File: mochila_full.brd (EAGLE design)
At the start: 100 x 80 mm, 13 parts, among them IC1 AD620R

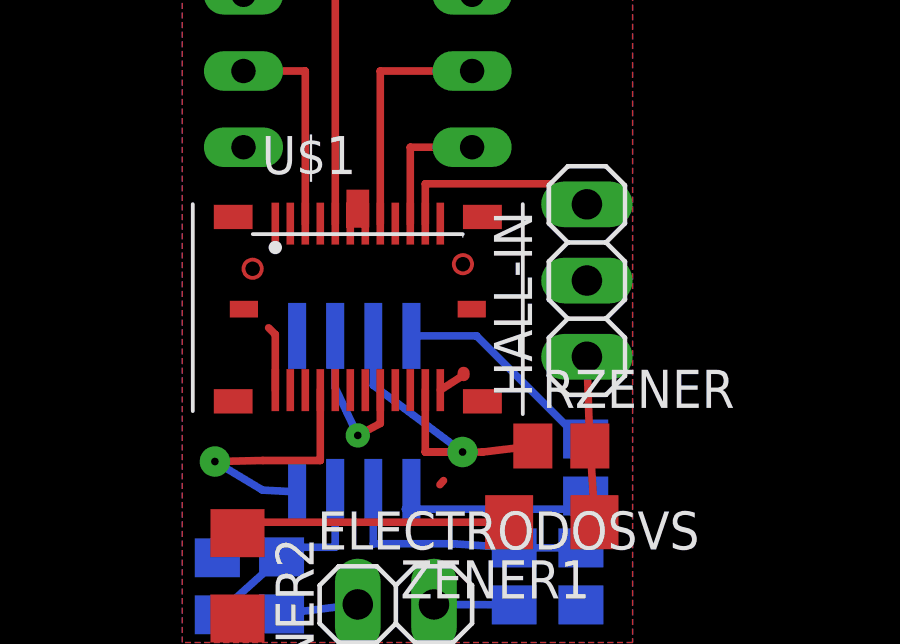
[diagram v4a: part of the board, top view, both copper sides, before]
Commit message: Usamos nueva libreria USBC
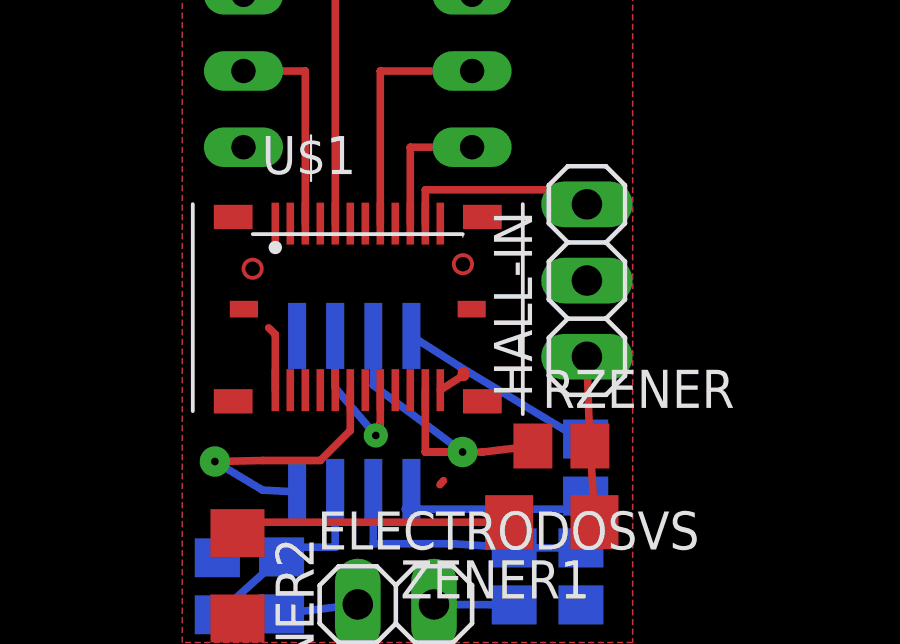
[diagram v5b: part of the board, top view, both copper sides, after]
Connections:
- removed net N$24: U$1.NC6
- net -12V: now also U$1.-12V; no longer U$1.-12VA, U$1.-12VB
- net EXTRA1: now also U$1.EXTRA1; no longer U$1.E1
- net EXTRA2: now also U$1.EXTRA2; no longer U$1.E2
- net N$12: now also U$1.ANULADA1; no longer U$1.CHECK1
- net N$13: now also U$1.ANULADA2; no longer U$1.CHECK2
- net N$25: now also U$1.EXTRA4; no longer U$1.NC5
- net NC2: now also U$1.EXTRA3C; no longer U$1.NC2
- net NC3: now also U$1.EXTRA3D; no longer U$1.NC4
- net OUTT: now also U$1.OUTT; no longer U$1.T
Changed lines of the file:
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@@
 <?xml version="1.0" encoding="utf-8"?>
 <!DOCTYPE eagle SYSTEM "eagle.dtd">
-<eagle version="9.2.2">
+<eagle version="7.7.0">
 <drawing>
 <settings>
 <setting alwaysvectorfont="no"/>
-<setting keepoldvectorfont="yes"/>
 <setting verticaltext="up"/>
 </settings>
@@
 <param name="dpMaxLengthDifference" value="10mm"/>
 <param name="dpGapFactor" value="2.5"/>
+<param name="checkGrid" value="0"/>
 <param name="checkAngle" value="0"/>
 <param name="checkFont" value="1"/>
 <param name="checkRestrict" value="1"/>
-<param name="checkStop" value="0"/>
-<param name="checkValues" value="0"/>
-<param name="checkNames" value="1"/>
-<param name="checkWireStubs" value="1"/>
-<param name="checkPolygonWidth" value="0"/>
 <param name="useDiameter" value="13"/>
 <param name="maxErrors" value="50"/>
@@
 <wire x1="37.5" y1="25.5" x2="36.7225" y2="30.4725" width="0" layer="19" extent="1-1"/>
 <wire x1="31.2225" y1="30.4725" x2="31" y2="27" width="0" layer="19" extent="1-1"/>
-<wire x1="41.41" y1="17.765" x2="36.83" y2="21.9075" width="0" layer="19" extent="1-16"/>
 </signal>
 <signal name="N$5">
@@
 <contactref element="IC1" pad="8"/>
 <wire x1="41.57" y1="23.2925" x2="41.37" y2="23.2925" width="0.254" layer="16"/>
-<wire x1="41.37" y1="23.2925" x2="37.9325" y2="26.73" width="0.254" layer="16"/>
-<wire x1="35.76" y1="26.73" x2="37.9325" y2="26.73" width="0.254" layer="16"/>
+<wire x1="41.37" y1="23.2925" x2="37.3325" y2="25.73" width="0.254" layer="16"/>
+<wire x1="35.76" y1="26.73" x2="37.3325" y2="25.73" width="0.254" layer="16"/>
 </signal>
 <signal name="+12V">
@@
 <signal name="-12V">
 <contactref element="IC1" pad="4"/>
-<contactref element="U$1" pad="-12VA"/>
-<contactref element="U$1" pad="-12VB"/>
 <wire x1="29.21" y1="22.5425" x2="30.81" y2="22.5775" width="0.254" layer="1"/>
 <wire x1="30.7975" y1="21.59" x2="29.21" y2="22.5425" width="0.254" layer="16"/>
 <wire x1="30.7975" y1="21.59" x2="31.95" y2="21.53" width="0.254" layer="16"/>
 <via x="29.21" y="22.5425" extent="1-16" drill="0.254" diameter="1.016" shape="square"/>
-<wire x1="32.7225" y1="24.9225" x2="32.7225" y2="22.5775" width="0.254" layer="1"/>
 <wire x1="32.7225" y1="22.5775" x2="30.81" y2="22.5775" width="0.254" layer="1"/>
-<wire x1="32.7225" y1="24.9225" x2="32.7225" y2="30.4725" width="0" layer="19" extent="1-1"/>
+<contactref element="U$1" pad="-12V"/>
+<wire x1="33.7225" y1="24.9225" x2="33.7225" y2="23.5775" width="0.254" layer="1"/>
+<wire x1="33.7225" y1="23.5775" x2="32.7225" y2="22.5775" width="0.254" layer="1"/>
 </signal>
 <signal name="OUTT">
 <contactref element="IC1" pad="6"/>
-<wire x1="33.22" y1="25" x2="33.9725" y2="23.4125" width="0.254" layer="16"/>
+<wire x1="33.22" y1="25" x2="34.5725" y2="23.4125" width="0.254" layer="16"/>
 <wire x1="33.22" y1="26.73" x2="33.22" y2="25" width="0.254" layer="16"/>
-<via x="33.9725" y="23.4125" extent="1-16" drill="0.254" diameter="0.8128" shape="square"/>
-<wire x1="33.9725" y1="23.4125" x2="34.7225" y2="23.8125" width="0.254" layer="1"/>
-<contactref element="U$1" pad="T"/>
+<via x="34.5725" y="23.4125" extent="1-16" drill="0.254" diameter="0.8128" shape="square"/>
+<wire x1="34.5725" y1="23.4125" x2="34.7225" y2="23.8125" width="0.254" layer="1"/>
+<contactref element="U$1" pad="OUTT"/>
 <wire x1="34.7225" y1="24.9225" x2="34.7225" y2="23.8125" width="0.254" layer="1"/>
 </signal>
@@
 </signal>
 <signal name="N$12">
-<contactref element="U$1" pad="CHECK1"/>
+<contactref element="U$1" pad="ANULADA1"/>
 </signal>
 <signal name="N$13">
-<contactref element="U$1" pad="CHECK2"/>
+<contactref element="U$1" pad="ANULADA2"/>
 </signal>
 <signal name="-I">
@@
 <contactref element="HALL-IN" pad="3"/>
 <contactref element="U$1" pad="HALL"/>
-<wire x1="36.2225" y1="30.4725" x2="36.2225" y2="31.8" width="0.254" layer="1"/>
-<wire x1="36.2225" y1="31.8" x2="40.4" y2="31.8" width="0.254" layer="1"/>
-<wire x1="40.4" y1="31.8" x2="40.4" y2="31.115" width="0.254" layer="1"/>
+<wire x1="36.2225" y1="30.4725" x2="36.2225" y2="31.6" width="0.254" layer="1"/>
+<wire x1="36.2225" y1="31.6" x2="40.4" y2="31.6" width="0.254" layer="1"/>
+<wire x1="40.4" y1="31.6" x2="40.4" y2="31.115" width="0.254" layer="1"/>
 <wire x1="40.4" y1="31.115" x2="41.61" y2="31.115" width="0.254" layer="1"/>
 </signal>
@@
 <contactref element="U$1" pad="NC7"/>
 </signal>
-<signal name="N$24">
-<contactref element="U$1" pad="NC6"/>
-</signal>
 <signal name="N$25">
-<contactref element="U$1" pad="NC5"/>
+<contactref element="U$1" pad="EXTRA4"/>
 </signal>
 <signal name="NC3">
-<contactref element="U$1" pad="NC4"/>
+<contactref element="U$1" pad="EXTRA3D"/>
 </signal>
 <signal name="+5V">
@@
 </signal>
 <signal name="EXTRA2">
-<contactref element="U$1" pad="E2"/>
+<contactref element="U$1" pad="EXTRA2"/>
 </signal>
 <signal name="NC2">
-<contactref element="U$1" pad="NC2"/>
+<contactref element="U$1" pad="EXTRA3C"/>
 </signal>
 <signal name="NC6">
@@
 </signal>
 <signal name="EXTRA1">
-<contactref element="U$1" pad="E1"/>
+<contactref element="U$1" pad="EXTRA1"/>
 </signal>
 </signals>
-<mfgpreviewcolors>
-<mfgpreviewcolor name="soldermaskcolor" color="0xC8008000"/>
-<mfgpreviewcolor name="silkscreencolor" color="0xFFFEFEFE"/>
-<mfgpreviewcolor name="backgroundcolor" color="0xFF282828"/>
-<mfgpreviewcolor name="coppercolor" color="0xFFFFBF00"/>
-<mfgpreviewcolor name="substratecolor" color="0xFF786E46"/>
-</mfgpreviewcolors>
 </board>
 </drawing>

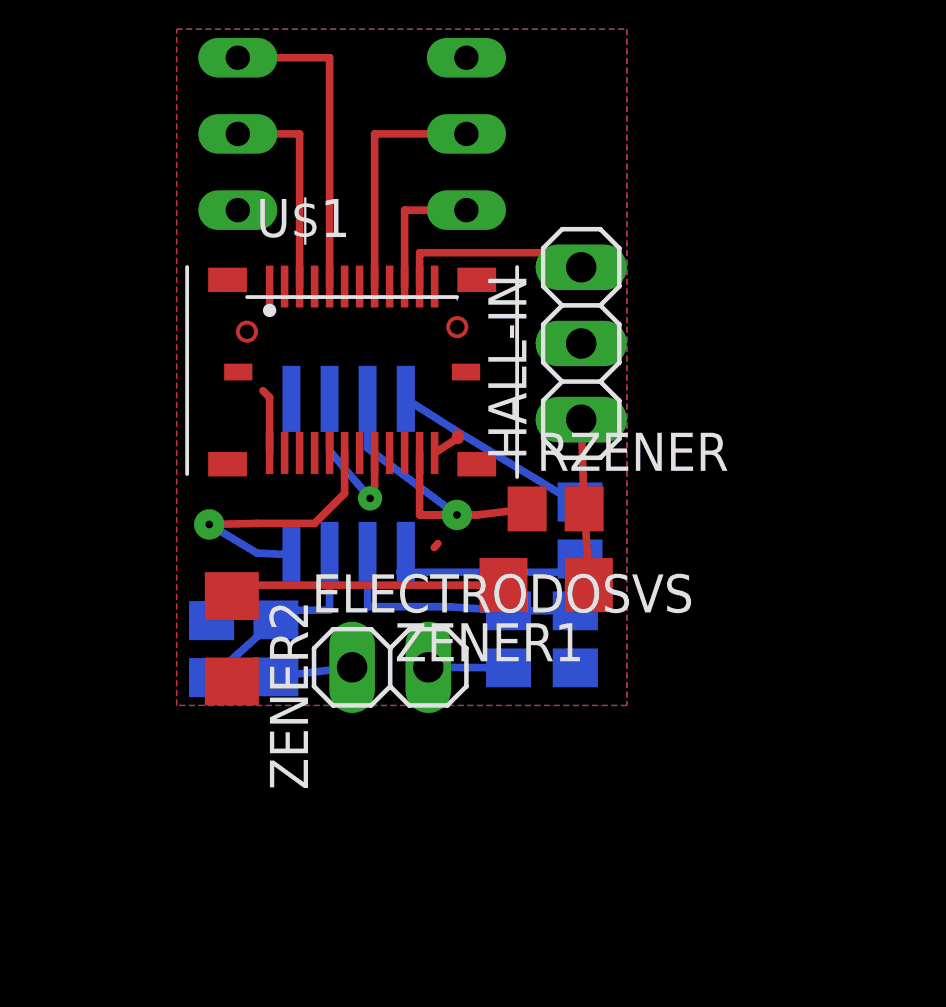
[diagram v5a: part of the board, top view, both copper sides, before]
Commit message: Version p/imprimir en masa
Reemplazo los zener por regulador 78L05

Agrego nombres y valores al layout
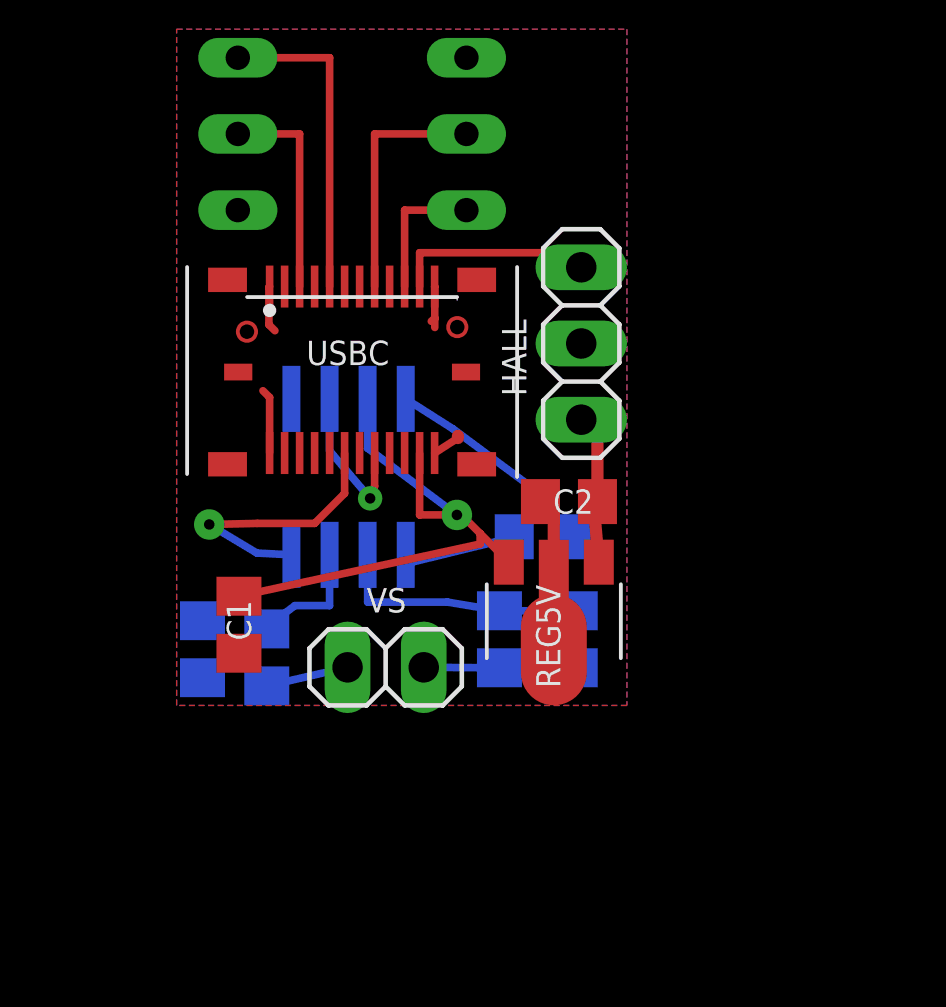
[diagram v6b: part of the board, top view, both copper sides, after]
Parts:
- removed CF1, CF2: (no value), eagle-ltspice:C0805
- removed ELECTRODOSVS: (no value), pinhead:1X02
- removed RF2, RZENER: (no value), eagle-ltspice:R0805
- removed ZENER1, ZENER2: (no value), eagle-ltspice:R1206
- added C1: 0.33u, rcl:C0805
- added C2: 0.1u, rcl:C0805
- added C3, C4: 10n, eagle-ltspice:C0805
- added R2: 100k, eagle-ltspice:R0805
- added REG5V: 78L05F, linear:SOT89
- added VS: (no value), pinhead:1X02
- R1: value (none) -> 100k
- RG: value (none) -> 220
- moved RG 1.26 mm to (40.3, 22.1), turned to 0 degrees
- renumbered FUJIKURASOCKET to FUJI, HALL-IN to HALL, RF1 to R1, U$1 to USBC
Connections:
- removed net N$8: ZENER1.2, ZENER2.1
- net +12V: now also C1.1, REG5V.3; no longer RZENER.1
- net +5V: now also C2.1, REG5V.1; no longer RZENER.2, ZENER1.1
- net GND: now also C1.2, C2.2, R2.1, REG5V.2; no longer RF2.1, ZENER2.2
- net N$1: now also C3.1, VS.1; no longer CF2.1, ELECTRODOSVS.1
- net N$2: now also C3.2, R2.2; no longer CF2.2, RF2.2
- net N$3: now also C4.1, VS.2; no longer CF1.1, ELECTRODOSVS.2
- net N$4: now also C4.2; no longer CF1.2
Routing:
- net N$8: track 9.67 -> 0.00 mm
- net +12V: track 12.3 -> 19.6 mm
- net GND: track 3.35 -> 8.76 mm
- net N$5: track 7.06 -> 3.91 mm

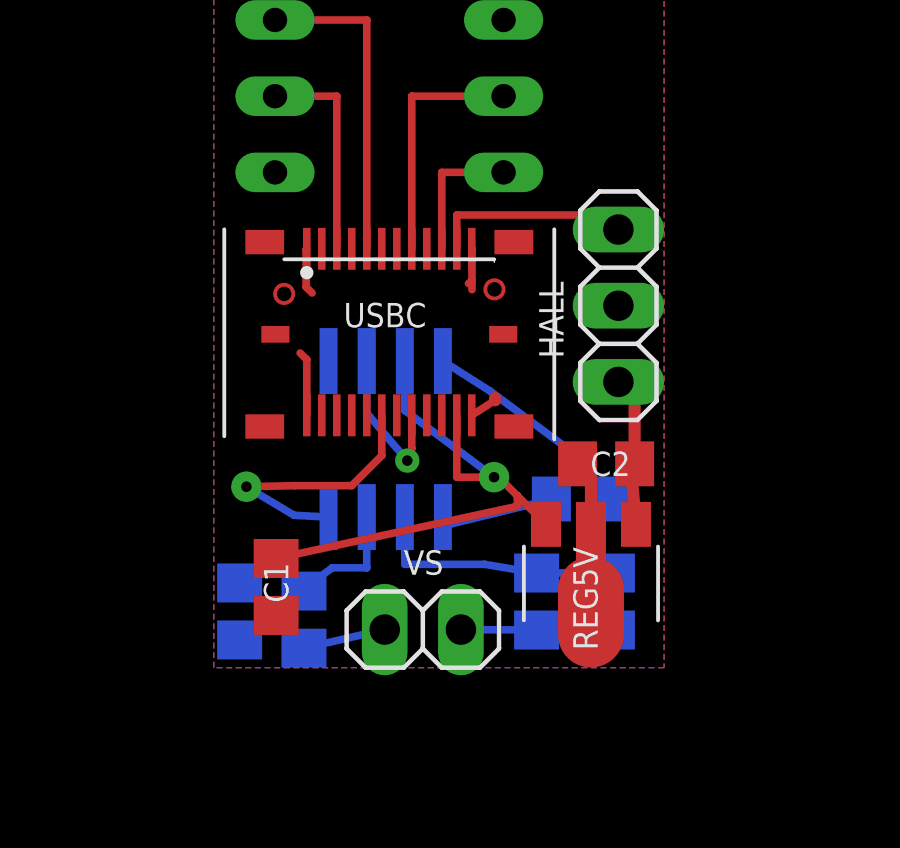
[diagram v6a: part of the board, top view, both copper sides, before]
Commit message: Version para imprimir de la mochila, con gerbers generados en .zip
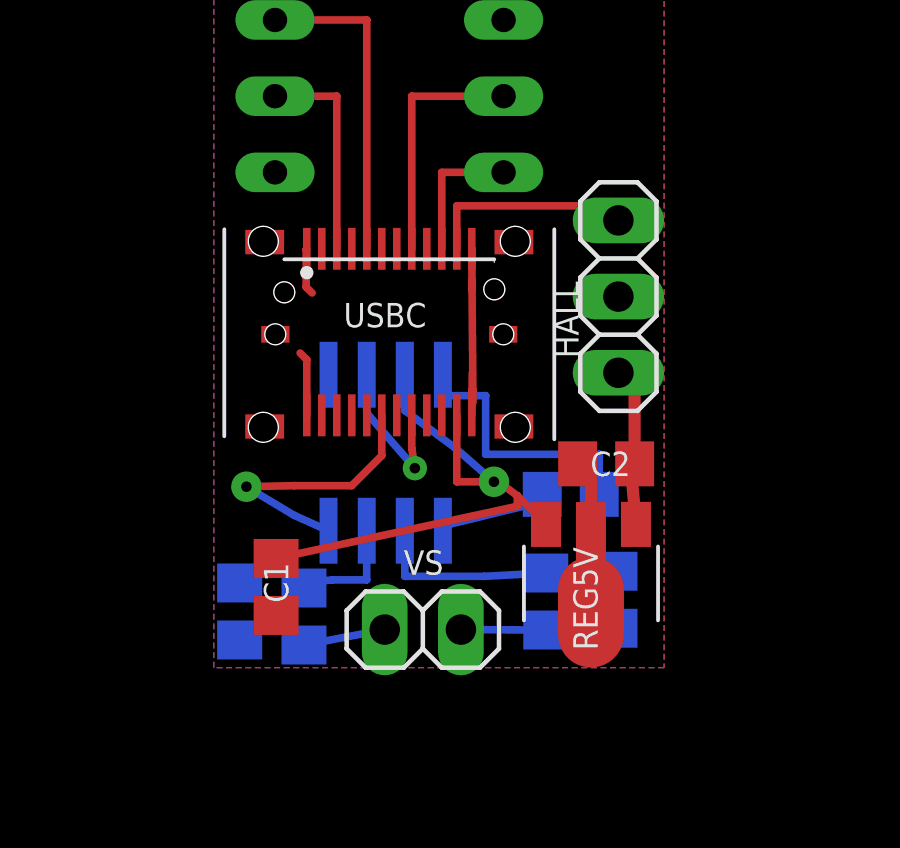
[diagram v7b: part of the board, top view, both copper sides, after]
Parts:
- moved IC1 0.46 mm to (33.9, 23.7)
- moved RG 0.34 mm to (40.0, 22.3)
- moved C4 0.30 mm to (39.2, 18.7)
- moved HALL 0.30 mm to (41.6, 28.9)
- moved C3 0.10 mm to (31.1, 18.2)
- moved R1 0.10 mm to (41.5, 18.8), turned to 90 degrees
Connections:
- net N$25: now also USBC.OUTHR; no longer USBC.EXTRA4
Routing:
- net GND: track 8.76 -> 13.1 mm
- net N$6: track 7.24 -> 9.15 mm
- net N$4: track 8.52 -> 9.17 mm

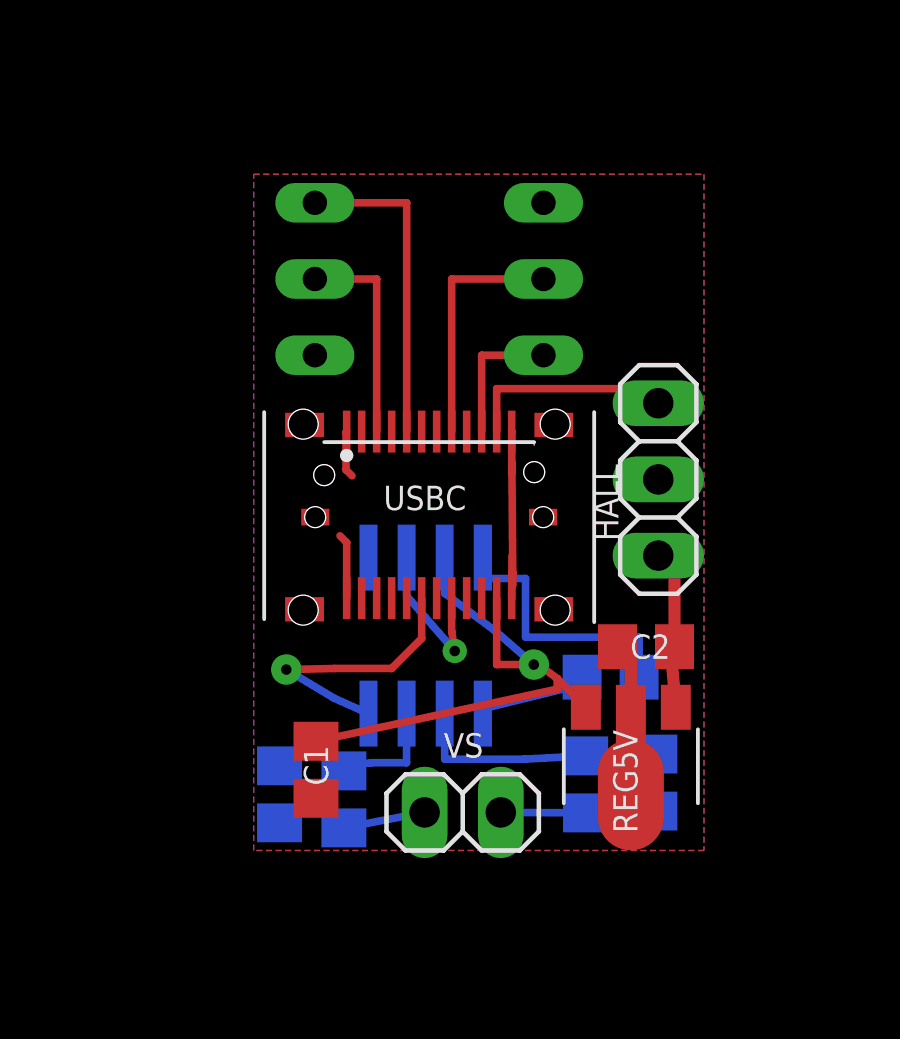
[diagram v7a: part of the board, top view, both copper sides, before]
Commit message: Agujeros de agarre del USB-C bien posicionados. No son agujeros, son PADS
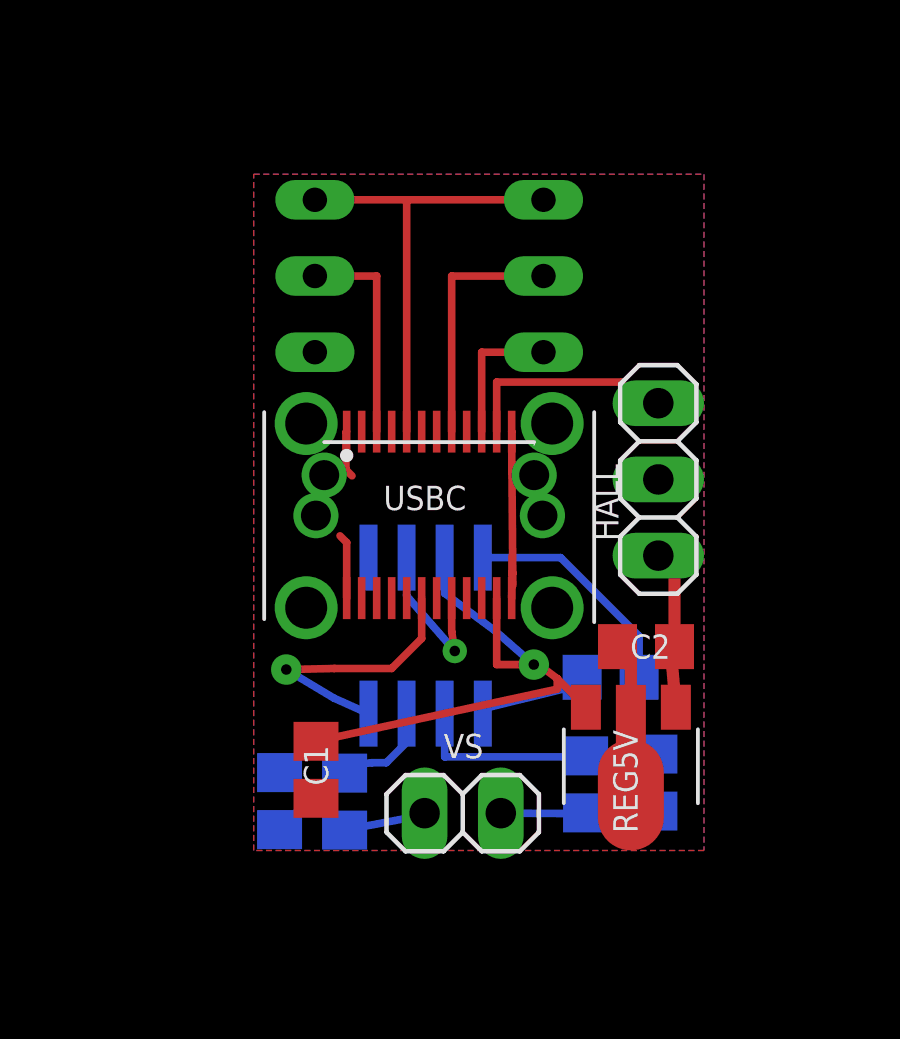
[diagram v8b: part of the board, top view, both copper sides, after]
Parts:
- moved R2 0.23 mm to (29.0, 18.2)
- moved FUJI 0.10 mm to (34.0, 35.7)
- moved C3 0.08 mm to (31.2, 18.1)
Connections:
- net GND: now also USBC.PATA1, USBC.PATA2, USBC.PATA3, USBC.PATA4, USBC.PATA5, USBC.PATA6, USBC.PATA7, USBC.PATA8
- net OUTP-: now also FUJI.1
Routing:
- net OUTP-: track 10.7 -> 15.3 mm
- net N$6: track 9.15 -> 8.36 mm
